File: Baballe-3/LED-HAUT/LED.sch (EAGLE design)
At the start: 24 parts, among them Q1 200mA/50V, Q2 200mA/50V, Q3 200mA/50V, Q4 200mA/50V

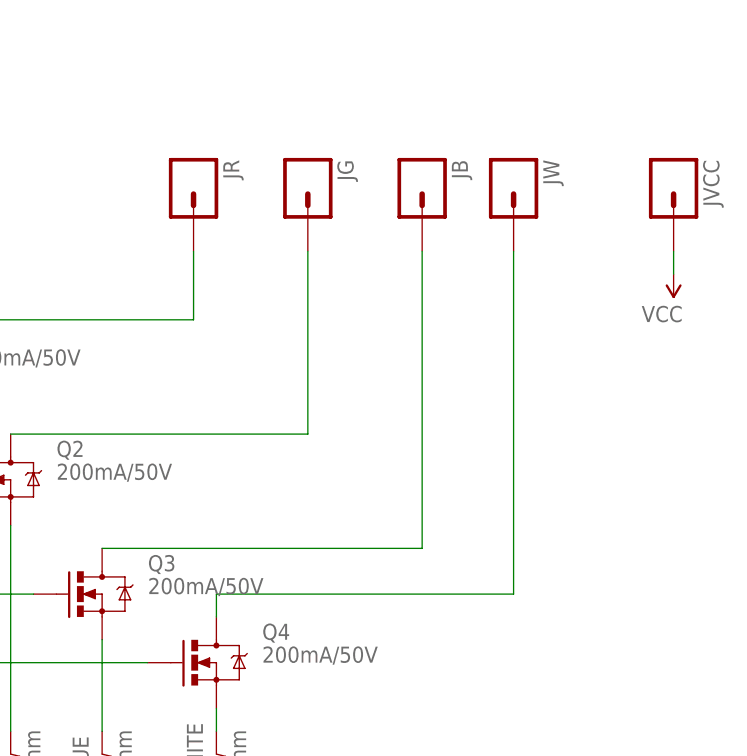
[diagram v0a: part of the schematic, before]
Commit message: Patch height error
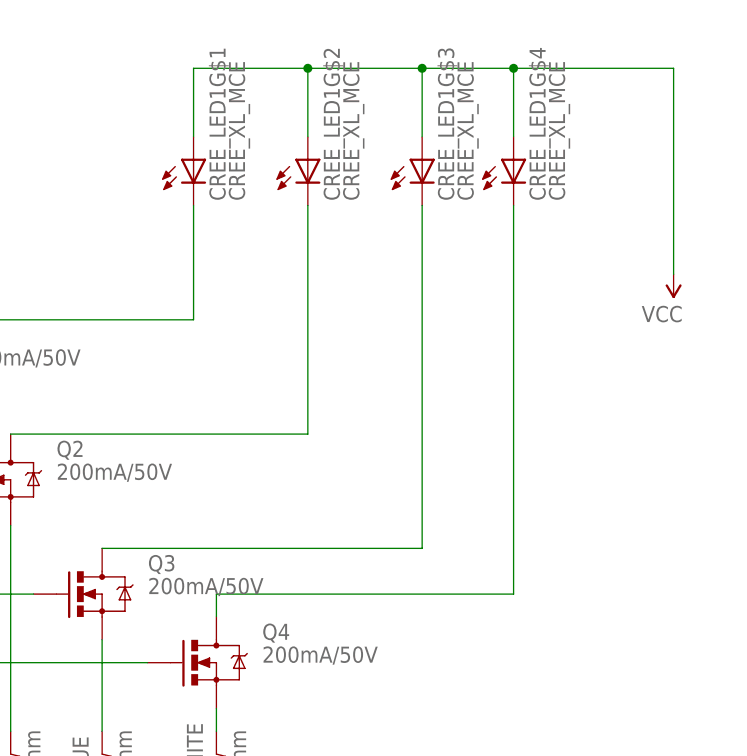
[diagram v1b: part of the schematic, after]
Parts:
- removed JB, JG, JR, JVCC, JW: (no value), SparkFun-Connectors:M01SMD
- added CREE_LED1: CREE_XL_MCE, CreeXL-MC-E:CREE_XL_MCE
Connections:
- net N$10: now also CREE_LED1G$1.C; no longer JR.1
- net N$11: now also CREE_LED1G$2.C; no longer JG.1
- net N$14: now also CREE_LED1G$4.C; no longer JW.1
- net N$9: now also CREE_LED1G$3.C; no longer JB.1
- net VCC: now also CREE_LED1G$1.A, CREE_LED1G$2.A, CREE_LED1G$3.A, CREE_LED1G$4.A; no longer JVCC.1
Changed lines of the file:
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@@
 <part name="RGW" library="SparkFun-Resistors" deviceset="RESISTOR" device="0805-RES" value="1KOhm"/>
 <part name="S1" library="SparkFun-Switches" deviceset="MOMENTARY-SWITCH-SPST" device="-PTH-RIGHT-ANGLE"/>
-<part name="JR" library="SparkFun-Connectors" deviceset="M01" device="SMD"/>
-<part name="JG" library="SparkFun-Connectors" deviceset="M01" device="SMD"/>
-<part name="JB" library="SparkFun-Connectors" deviceset="M01" device="SMD"/>
-<part name="JW" library="SparkFun-Connectors" deviceset="M01" device="SMD"/>
-<part name="JVCC" library="SparkFun-Connectors" deviceset="M01" device="SMD"/>
+<part name="CREE_LED1" library="CreeXL-MC-E" deviceset="CREE_XL_MCE" device=""/>
 </parts>
 <sheets>
@@
 <instance part="RGW" gate="G$1" x="-20.32" y="50.8"/>
 <instance part="S1" gate="G$1" x="-50.8" y="76.2"/>
-<instance part="JR" gate="G$1" x="33.02" y="68.58" rot="R270"/>
-<instance part="JG" gate="G$1" x="45.72" y="68.58" rot="R270"/>
-<instance part="JB" gate="G$1" x="58.42" y="68.58" rot="R270"/>
-<instance part="JW" gate="G$1" x="68.58" y="68.58" rot="R270"/>
-<instance part="JVCC" gate="G$1" x="86.36" y="68.58" rot="R270"/>
+<instance part="CREE_LED1" gate="G$1" x="33.02" y="71.12"/>
+<instance part="CREE_LED1" gate="G$2" x="45.72" y="71.12"/>
+<instance part="CREE_LED1" gate="G$3" x="58.42" y="71.12"/>
+<instance part="CREE_LED1" gate="G$4" x="68.58" y="71.12"/>
 </instances>
 <busses>
@@
 <pinref part="Q3" gate="G$1" pin="D"/>
 <wire x1="22.86" y1="27.94" x2="58.42" y2="27.94" width="0.1524" layer="91"/>
-<wire x1="58.42" y1="27.94" x2="58.42" y2="60.96" width="0.1524" layer="91"/>
-<pinref part="JB" gate="G$1" pin="1"/>
+<wire x1="58.42" y1="27.94" x2="58.42" y2="66.04" width="0.1524" layer="91"/>
+<pinref part="CREE_LED1" gate="G$3" pin="C"/>
 </segment>
 </net>
@@
 <pinref part="Q1" gate="G$1" pin="D"/>
 <wire x1="2.54" y1="53.34" x2="33.02" y2="53.34" width="0.1524" layer="91"/>
-<wire x1="33.02" y1="60.96" x2="33.02" y2="53.34" width="0.1524" layer="91"/>
-<pinref part="JR" gate="G$1" pin="1"/>
+<wire x1="33.02" y1="66.04" x2="33.02" y2="53.34" width="0.1524" layer="91"/>
+<pinref part="CREE_LED1" gate="G$1" pin="C"/>
 </segment>
 </net>
 <net name="N$11" class="2">
 <segment>
-<wire x1="45.72" y1="60.96" x2="45.72" y2="40.64" width="0.1524" layer="91"/>
+<wire x1="45.72" y1="66.04" x2="45.72" y2="40.64" width="0.1524" layer="91"/>
 <pinref part="Q2" gate="G$1" pin="D"/>
 <wire x1="45.72" y1="40.64" x2="12.7" y2="40.64" width="0.1524" layer="91"/>
-<pinref part="JG" gate="G$1" pin="1"/>
+<pinref part="CREE_LED1" gate="G$2" pin="C"/>
 </segment>
 </net>
@@
 </segment>
 <segment>
-<pinref part="JVCC" gate="G$1" pin="1"/>
 <pinref part="SUPPLY1" gate="G$1" pin="VCC"/>
-<wire x1="86.36" y1="60.96" x2="86.36" y2="58.42" width="0.1524" layer="91"/>
+<pinref part="CREE_LED1" gate="G$1" pin="A"/>
+<wire x1="33.02" y1="73.66" x2="33.02" y2="81.28" width="0.1524" layer="91"/>
+<wire x1="33.02" y1="81.28" x2="45.72" y2="81.28" width="0.1524" layer="91"/>
+<wire x1="45.72" y1="81.28" x2="58.42" y2="81.28" width="0.1524" layer="91"/>
+<wire x1="58.42" y1="81.28" x2="68.58" y2="81.28" width="0.1524" layer="91"/>
+<wire x1="68.58" y1="81.28" x2="86.36" y2="81.28" width="0.1524" layer="91"/>
+<wire x1="86.36" y1="81.28" x2="86.36" y2="58.42" width="0.1524" layer="91"/>
+<pinref part="CREE_LED1" gate="G$4" pin="A"/>
+<wire x1="68.58" y1="73.66" x2="68.58" y2="81.28" width="0.1524" layer="91"/>
+<pinref part="CREE_LED1" gate="G$3" pin="A"/>
+<wire x1="58.42" y1="73.66" x2="58.42" y2="81.28" width="0.1524" layer="91"/>
+<pinref part="CREE_LED1" gate="G$2" pin="A"/>
+<wire x1="45.72" y1="73.66" x2="45.72" y2="81.28" width="0.1524" layer="91"/>
+<junction x="45.72" y="81.28"/>
+<junction x="58.42" y="81.28"/>
+<junction x="68.58" y="81.28"/>
 </segment>
 </net>
@@
 <wire x1="35.56" y1="20.32" x2="35.56" y2="22.86" width="0.1524" layer="91"/>
 <wire x1="35.56" y1="22.86" x2="68.58" y2="22.86" width="0.1524" layer="91"/>
-<wire x1="68.58" y1="22.86" x2="68.58" y2="60.96" width="0.1524" layer="91"/>
-<pinref part="JW" gate="G$1" pin="1"/>
-</segment>
-</net>
+<wire x1="68.58" y1="22.86" x2="68.58" y2="66.04" width="0.1524" layer="91"/>
+<pinref part="CREE_LED1" gate="G$4" pin="C"/>
+</segment>
+</net>
